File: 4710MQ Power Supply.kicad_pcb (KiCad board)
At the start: 2 copper layers, 40 x 47.5 mm, 20 parts, among them J1 Jack-DC, J2 ATX 4 Pin, J3 Molex 4 Pin, U1 MP1499GD-Z

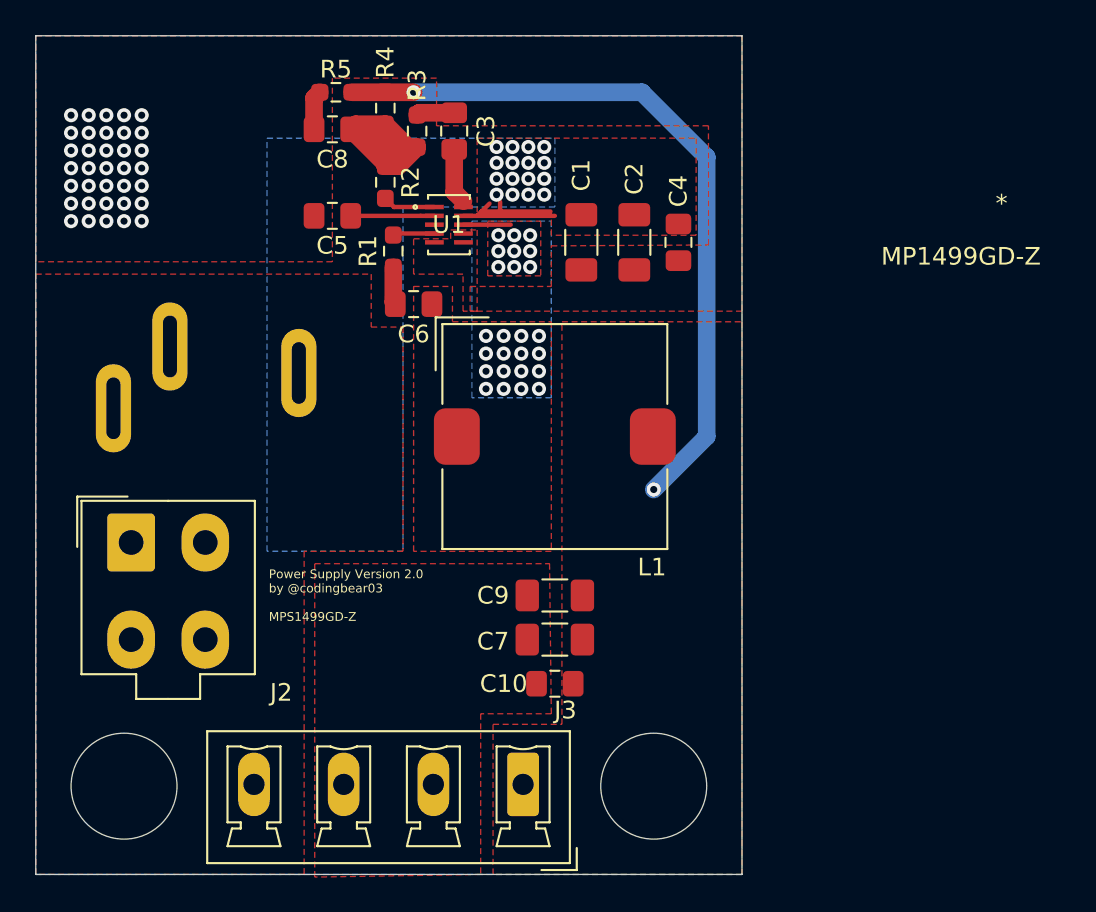
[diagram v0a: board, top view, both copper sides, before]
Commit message: Version 3.0
- Added Current Sensor
- Added Thermometer IC
- Added 2.54 pitch 4pin output
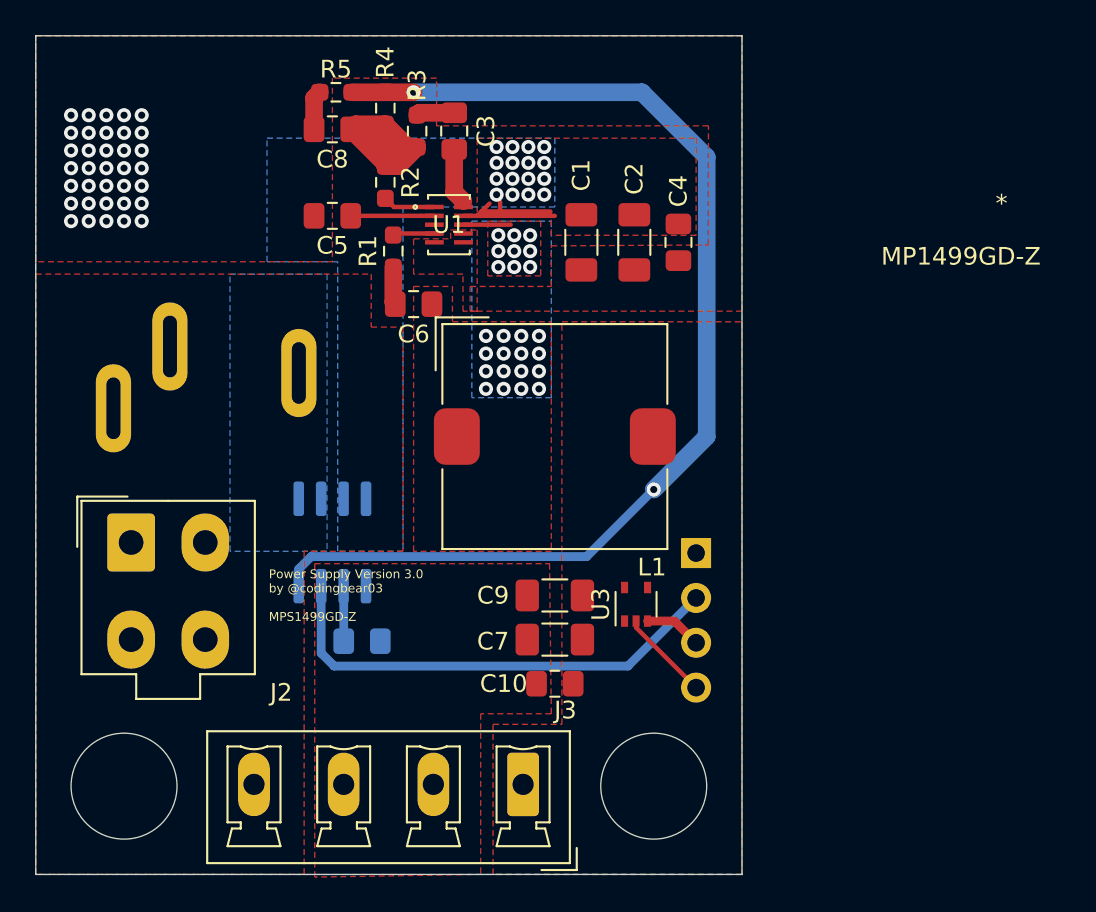
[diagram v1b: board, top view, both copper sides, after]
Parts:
- added C11: 1nF, Capacitor_SMD:C_0805_2012Metric_Pad1.18x1.45mm_HandSolder, B.Cu at (138.5, 115.8)
- added J4: Conn_01x04, Connector_PinSocket_2.54mm:PinSocket_1x04_P2.54mm_Vertical, B.Cu at (157.4, 110.8)
- added U2: ACS712xLCTR-30A, Package_SO:SOIC-8_3.9x4.9mm_P1.27mm, B.Cu at (136.8, 110.2)
- added U3: MCP9700T-ELT, Package_TO_SOT_SMD:SOT-353_SC-70-5, F.Cu at (154.0, 113.7)
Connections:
- J1 pad 1: +12V -> VDC
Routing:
- net /CURR_OUT: track 0.00 -> 26.9 mm
- net +5V: track 41.7 -> 64.6 mm
- net GND: track 2.15 -> 7.33 mm
- net /TEMP_OUT: track 0.00 -> 3.26 mm
- net Net-(C11-Pad1): track 0.00 -> 3.12 mm
- added copper zone on B.Cu, net VDC
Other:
- board text added: "Power Supply Version 3.0 by @codingbear03 MPS1499GD-Z"
- board text removed: "Power Supply Version 2.0 by @codingbear03 MPS1499GD-Z"
